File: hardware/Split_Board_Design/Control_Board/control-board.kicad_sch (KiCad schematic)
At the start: 12 parts, among them J10 Conn_01x03, J2 UART_CONN, J3 XT30PW-M, J5 Conn_01x06, J7 Conn_01x03, J8 Conn_01x03, J9 Conn_01x02

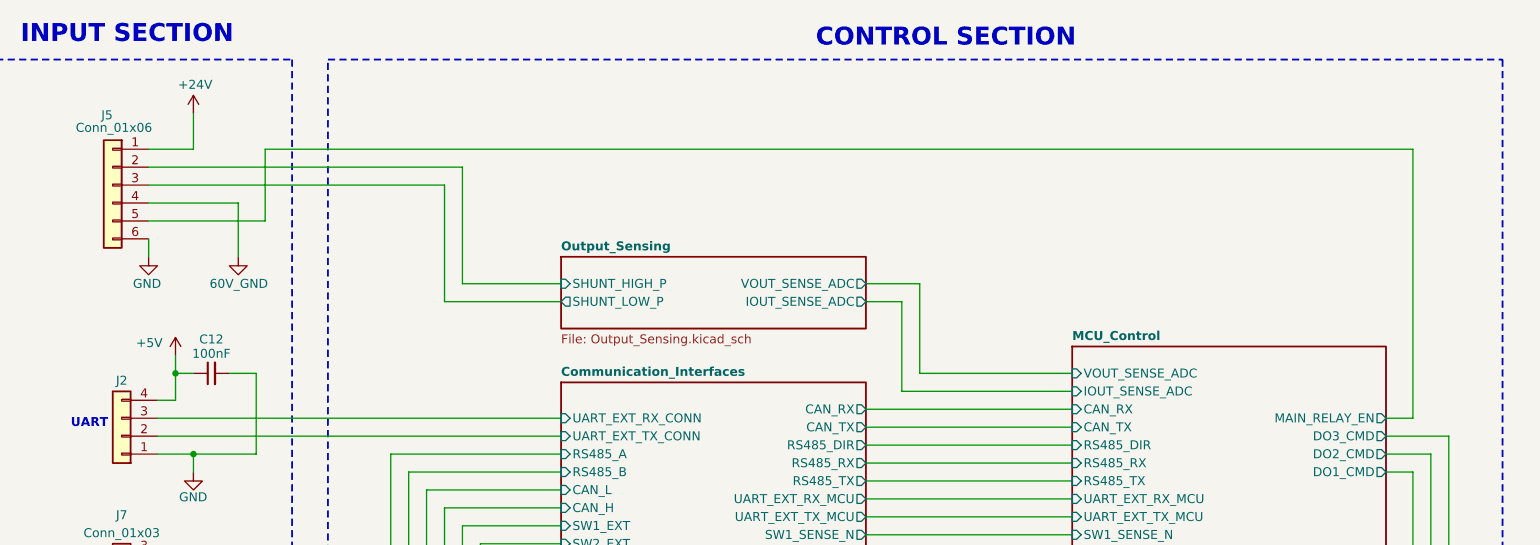
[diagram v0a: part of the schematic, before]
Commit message: feat(layout): Finished demo schematic for control board
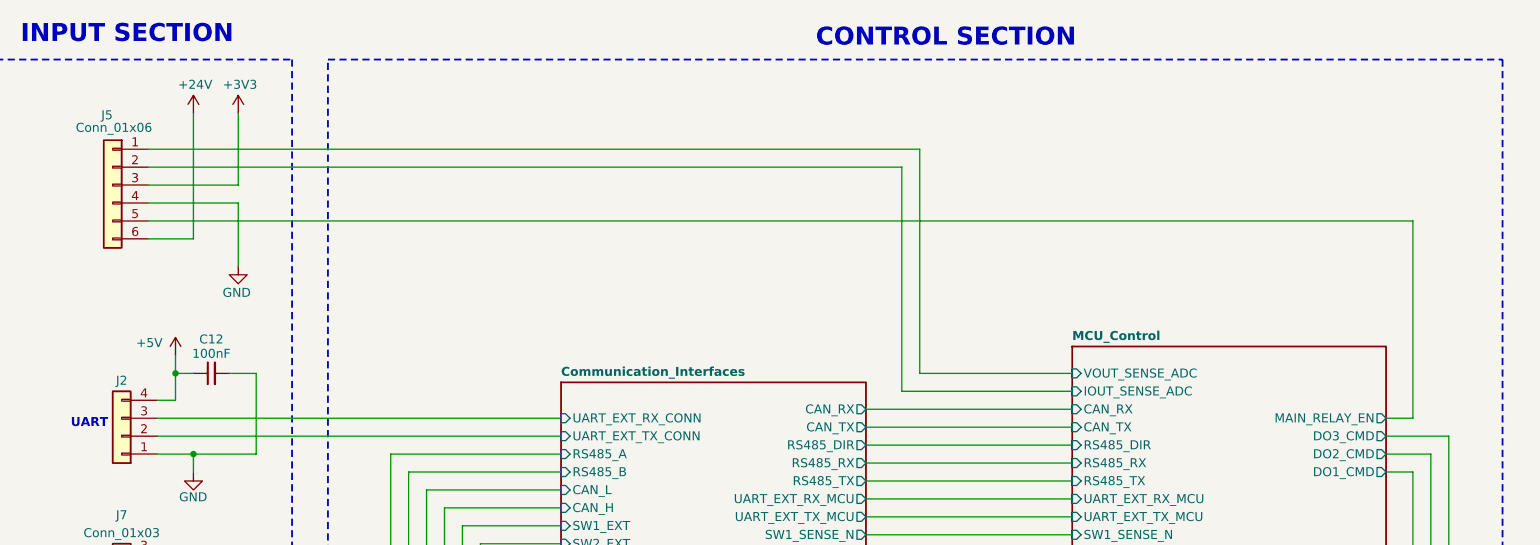
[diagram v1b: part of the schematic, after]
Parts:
- J10, J7: footprint Connector_Phoenix_MC:PhoenixContact_MC_1,5_3-G-3.5_1x03_P3.50mm_Horizontal -> Connector_Phoenix_MC:PhoenixContact_MC_1,5_3-G-3.81_1x03_P3.81mm_Horizontal; Link to Buy (none) -> https://linhkien.cxtvn.com/3486-cau-dau-15edg381-381mm-xanh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
- J5: Link to Buy (none) -> https://linhkien.cxtvn.com/3878-header-duc-xh254-6p-chan-co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
- J8, J9: Link to Buy (none) -> https://linhkien.cxtvn.com/3486-cau-dau-15edg381-381mm-xanh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
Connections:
- net 60V_GND is gone; now on net GND: J5.4 (Pin_4)
- net Output_Sensing/SHUNT_HIGH_P is gone; now on net MCU_Control/IOUT_SENSE_ADC: J5.2 (Pin_2)
- net Output_Sensing/SHUNT_LOW_P is gone; now on net +3V3: J5.3 (Pin_3)
- net +24V: now also J5.6 (Pin_6); no longer J5.1 (Pin_1)
- net GND: no longer J5.6 (Pin_6)
- net MCU_Control/VOUT_SENSE_ADC: now also J5.1 (Pin_1)
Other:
- removed sheet Output_Sensing

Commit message: feat(layout): Update layout
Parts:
- C12: value 100nF -> 100nF-50V; footprint Capacitor_SMD:C_0805_2012Metric -> Capacitor_SMD:C_0603_1608Metric; Link to Buy https://linhkien.cxtvn.com/1976-tu-khong-phan-cuc-0805.html -> https://linhkien.cxtvn.com/1981-tu-0603-khong-phan-cuc.html
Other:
- moved on the sheet: H4, H5, H6, H7
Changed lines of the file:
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@@
 	(wire
 		(pts
-			(xy 146.05 38.1) (xy 36.83 38.1)
+			(xy 153.67 38.1) (xy 36.83 38.1)
 		)
 		(stroke
@@
 	(wire
 		(pts
-			(xy 143.51 72.39) (xy 167.64 72.39)
+			(xy 151.13 72.39) (xy 167.64 72.39)
 		)
 		(stroke
@@
 	(wire
 		(pts
-			(xy 146.05 69.85) (xy 167.64 69.85)
+			(xy 153.67 69.85) (xy 167.64 69.85)
 		)
 		(stroke
@@
 	(wire
 		(pts
-			(xy 143.51 40.64) (xy 143.51 72.39)
+			(xy 151.13 40.64) (xy 151.13 72.39)
 		)
 		(stroke
@@
 	(wire
 		(pts
-			(xy 143.51 40.64) (xy 36.83 40.64)
+			(xy 151.13 40.64) (xy 36.83 40.64)
 		)
 		(stroke
@@
 	(wire
 		(pts
-			(xy 146.05 38.1) (xy 146.05 69.85)
+			(xy 153.67 38.1) (xy 153.67 69.85)
 		)
 		(stroke
@@
 	(symbol
 		(lib_id "Mechanical:MountingHole")
-		(at 99.06 173.99 0)
+		(at 99.06 182.88 0)
 		(unit 1)
 		(body_style 1)
@@
 		(fields_autoplaced yes)
 		(property "Reference" "H7"
-			(at 101.6 172.7199 0)
+			(at 101.6 181.6099 0)
 			(show_name no)
 			(do_not_autoplace no)
@@
 		)
 		(property "Value" "MountingHole"
-			(at 101.6 175.2599 0)
+			(at 101.6 184.1499 0)
 			(show_name no)
 			(do_not_autoplace no)
@@
 		)
 		(property "Footprint" "MountingHole:MountingHole_3.2mm_M3"
-			(at 99.06 173.99 0)
+			(at 99.06 182.88 0)
 			(hide yes)
 			(show_name no)
@@
 		)
 		(property "Datasheet" ""
-			(at 99.06 173.99 0)
+			(at 99.06 182.88 0)
 			(hide yes)
 			(show_name no)
@@
 		)
 		(property "Description" "Mounting Hole without connection"
-			(at 99.06 173.99 0)
+			(at 99.06 182.88 0)
 			(hide yes)
 			(show_name no)
@@
 		)
 		(property "CREATOR" ""
-			(at 99.06 173.99 0)
+			(at 99.06 182.88 0)
 			(hide yes)
 			(show_name no)
@@
 	(symbol
 		(lib_id "Mechanical:MountingHole")
-		(at 157.48 173.99 0)
+		(at 157.48 182.88 0)
 		(unit 1)
 		(body_style 1)
@@
 		(fields_autoplaced yes)
 		(property "Reference" "H4"
-			(at 160.02 172.7199 0)
+			(at 160.02 181.6099 0)
 			(show_name no)
 			(do_not_autoplace no)
@@
 		)
 		(property "Value" "MountingHole"
-			(at 160.02 175.2599 0)
+			(at 160.02 184.1499 0)
 			(show_name no)
 			(do_not_autoplace no)
@@
 		)
 		(property "Footprint" "MountingHole:MountingHole_3.2mm_M3"
-			(at 157.48 173.99 0)
+			(at 157.48 182.88 0)
 			(hide yes)
 			(show_name no)
@@
 		)
 		(property "Datasheet" ""
-			(at 157.48 173.99 0)
+			(at 157.48 182.88 0)
 			(hide yes)
 			(show_name no)
@@
 		)
 		(property "Description" "Mounting Hole without connection"
-			(at 157.48 173.99 0)
+			(at 157.48 182.88 0)
 			(hide yes)
 			(show_name no)
@@
 		)
 		(property "CREATOR" ""
-			(at 157.48 173.99 0)
+			(at 157.48 182.88 0)
 			(hide yes)
 			(show_name no)
@@
 	(symbol
 		(lib_id "Mechanical:MountingHole")
-		(at 118.11 173.99 0)
+		(at 118.11 182.88 0)
 		(unit 1)
 		(body_style 1)
@@
 		(fields_autoplaced yes)
 		(property "Reference" "H6"
-			(at 120.65 172.7199 0)
+			(at 120.65 181.6099 0)
 			(show_name no)
 			(do_not_autoplace no)
@@
 		)
 		(property "Value" "MountingHole"
-			(at 120.65 175.2599 0)
+			(at 120.65 184.1499 0)
 			(show_name no)
 			(do_not_autoplace no)
@@
 		)
 		(property "Footprint" "MountingHole:MountingHole_3.2mm_M3"
-			(at 118.11 173.99 0)
+			(at 118.11 182.88 0)
 			(hide yes)
 			(show_name no)
@@
 		)
 		(property "Datasheet" ""
-			(at 118.11 173.99 0)
+			(at 118.11 182.88 0)
 			(hide yes)
 			(show_name no)
@@
 		)
 		(property "Description" "Mounting Hole without connection"
-			(at 118.11 173.99 0)
+			(at 118.11 182.88 0)
 			(hide yes)
 			(show_name no)
@@
 		)
 		(property "CREATOR" ""
-			(at 118.11 173.99 0)
+			(at 118.11 182.88 0)
 			(hide yes)
 			(show_name no)
@@
 			)
 		)
-		(property "Value" "100nF"
+		(property "Value" "100nF-50V"
 			(at 45.72 67.056 90)
 			(show_name no)
@@
 			)
 		)
-		(property "Footprint" "Capacitor_SMD:C_0805_2012Metric"
+		(property "Footprint" "Capacitor_SMD:C_0603_1608Metric"
 			(at 45.72 69.85 0)
 			(hide yes)
@@
 			)
 		)
-		(property "Link to Buy" "https://linhkien.cxtvn.com/1976-tu-khong-phan-cuc-0805.html"
+		(property "Link to Buy" "https://linhkien.cxtvn.com/1981-tu-0603-khong-phan-cuc.html"
 			(at -80.01 179.07 0)
 			(hide yes)
@@
 	(symbol
 		(lib_id "Mechanical:MountingHole")
-		(at 137.16 173.99 0)
+		(at 137.16 182.88 0)
 		(unit 1)
 		(body_style 1)
@@
 		(fields_autoplaced yes)
 		(property "Reference" "H5"
-			(at 139.7 172.7199 0)
+			(at 139.7 181.6099 0)
 			(show_name no)
 			(do_not_autoplace no)
@@
 		)
 		(property "Value" "MountingHole"
-			(at 139.7 175.2599 0)
+			(at 139.7 184.1499 0)
 			(show_name no)
 			(do_not_autoplace no)
@@
 		)
 		(property "Footprint" "MountingHole:MountingHole_3.2mm_M3"
-			(at 137.16 173.99 0)
+			(at 137.16 182.88 0)
 			(hide yes)
 			(show_name no)
@@
 		)
 		(property "Datasheet" ""
-			(at 137.16 173.99 0)
+			(at 137.16 182.88 0)
 			(hide yes)
 			(show_name no)
@@
 		)
 		(property "Description" "Mounting Hole without connection"
-			(at 137.16 173.99 0)
+			(at 137.16 182.88 0)
 			(hide yes)
 			(show_name no)
@@
 		)
 		(property "CREATOR" ""
-			(at 137.16 173.99 0)
+			(at 137.16 182.88 0)
 			(hide yes)
 			(show_name no)

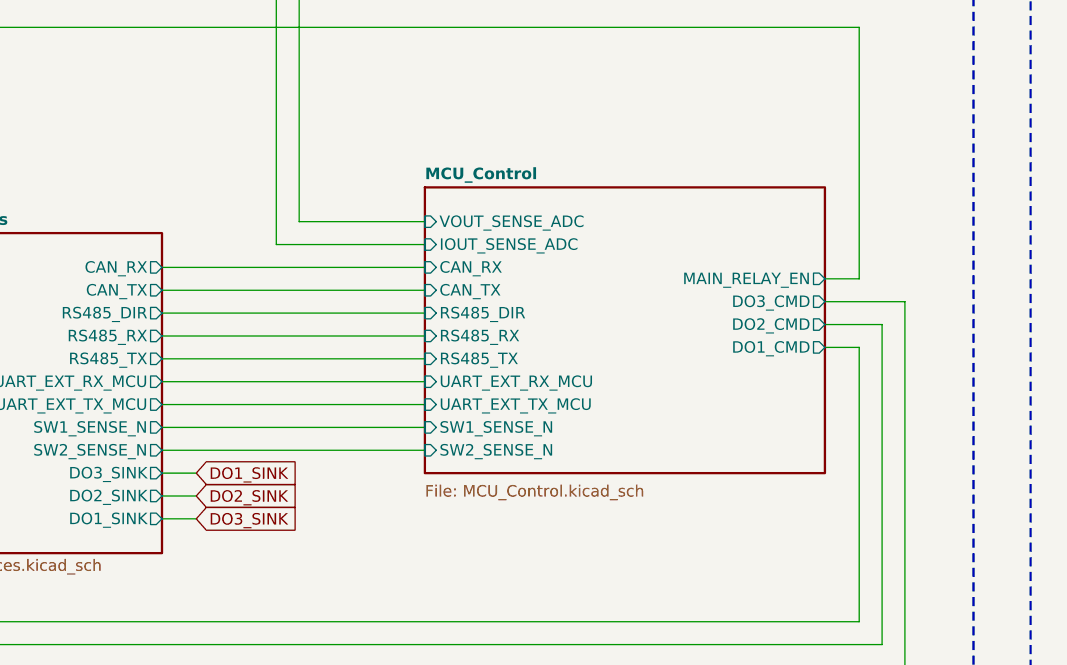
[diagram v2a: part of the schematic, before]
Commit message: feat(layout): update control board layout
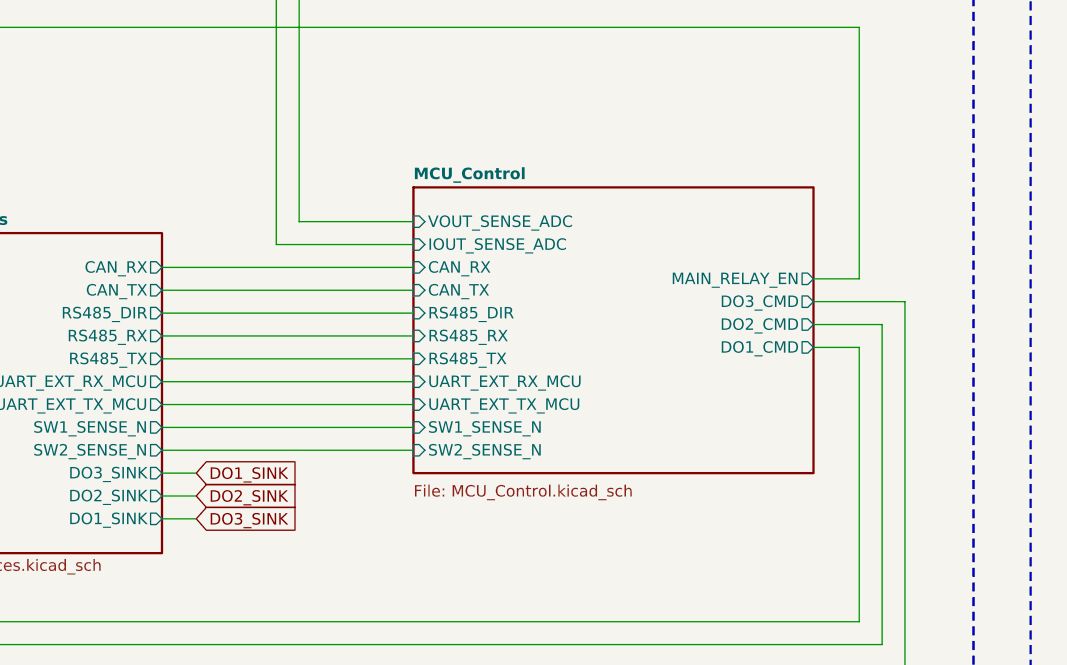
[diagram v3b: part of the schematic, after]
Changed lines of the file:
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@@
 	(wire
 		(pts
-			(xy 212.09 78.74) (xy 220.98 78.74)
+			(xy 210.82 78.74) (xy 220.98 78.74)
 		)
 		(stroke
@@
 	(wire
 		(pts
-			(xy 151.13 72.39) (xy 167.64 72.39)
+			(xy 151.13 72.39) (xy 166.37 72.39)
 		)
 		(stroke
@@
 	(wire
 		(pts
-			(xy 167.64 80.01) (xy 138.43 80.01)
+			(xy 166.37 80.01) (xy 138.43 80.01)
 		)
 		(stroke
@@
 	(wire
 		(pts
-			(xy 153.67 69.85) (xy 167.64 69.85)
+			(xy 153.67 69.85) (xy 166.37 69.85)
 		)
 		(stroke
@@
 	(wire
 		(pts
-			(xy 167.64 85.09) (xy 138.43 85.09)
+			(xy 166.37 85.09) (xy 138.43 85.09)
 		)
 		(stroke
@@
 	(wire
 		(pts
-			(xy 167.64 82.55) (xy 138.43 82.55)
+			(xy 166.37 82.55) (xy 138.43 82.55)
 		)
 		(stroke
@@
 	(wire
 		(pts
-			(xy 215.9 76.2) (xy 212.09 76.2)
+			(xy 215.9 76.2) (xy 210.82 76.2)
 		)
 		(stroke
@@
 	(wire
 		(pts
-			(xy 167.64 92.71) (xy 138.43 92.71)
+			(xy 166.37 92.71) (xy 138.43 92.71)
 		)
 		(stroke
@@
 	(wire
 		(pts
-			(xy 167.64 95.25) (xy 138.43 95.25)
+			(xy 166.37 95.25) (xy 138.43 95.25)
 		)
 		(stroke
@@
 	(wire
 		(pts
-			(xy 167.64 74.93) (xy 138.43 74.93)
+			(xy 166.37 74.93) (xy 138.43 74.93)
 		)
 		(stroke
@@
 	(wire
 		(pts
-			(xy 167.64 87.63) (xy 138.43 87.63)
+			(xy 166.37 87.63) (xy 138.43 87.63)
 		)
 		(stroke
@@
 	(wire
 		(pts
-			(xy 212.09 81.28) (xy 218.44 81.28)
+			(xy 210.82 81.28) (xy 218.44 81.28)
 		)
 		(stroke
@@
 	(wire
 		(pts
-			(xy 212.09 83.82) (xy 215.9 83.82)
+			(xy 210.82 83.82) (xy 215.9 83.82)
 		)
 		(stroke
@@
 	(wire
 		(pts
-			(xy 167.64 77.47) (xy 138.43 77.47)
+			(xy 166.37 77.47) (xy 138.43 77.47)
 		)
 		(stroke
@@
 	(wire
 		(pts
-			(xy 167.64 90.17) (xy 138.43 90.17)
+			(xy 166.37 90.17) (xy 138.43 90.17)
 		)
 		(stroke
@@
 	)
 	(sheet
-		(at 167.64 66.04)
+		(at 166.37 66.04)
 		(size 44.45 31.75)
 		(exclude_from_sim no)
@@
 		)
 		(property "Sheetname" "MCU_Control"
-			(at 167.64 65.2776 0)
+			(at 166.37 65.2776 0)
 			(show_name no)
 			(do_not_autoplace no)
@@
 		)
 		(property "Sheetfile" "MCU_Control.kicad_sch"
-			(at 167.64 99.06 0)
+			(at 166.37 99.06 0)
 			(show_name no)
 			(do_not_autoplace no)
@@
 		)
 		(pin "IOUT_SENSE_ADC" input
-			(at 167.64 72.39 180)
+			(at 166.37 72.39 180)
 			(effects
 				(font
@@
 		)
 		(pin "MAIN_RELAY_EN" output
-			(at 212.09 76.2 0)
+			(at 210.82 76.2 0)
 			(effects
 				(font
@@
 		)
 		(pin "VOUT_SENSE_ADC" input
-			(at 167.64 69.85 180)
+			(at 166.37 69.85 180)
 			(effects
 				(font
@@
 		)
 		(pin "CAN_RX" input
-			(at 167.64 74.93 180)
+			(at 166.37 74.93 180)
 			(effects
 				(font
@@
 		)
 		(pin "RS485_DIR" input
-			(at 167.64 80.01 180)
+			(at 166.37 80.01 180)
 			(effects
 				(font
@@
 		)
 		(pin "CAN_TX" input
-			(at 167.64 77.47 180)
+			(at 166.37 77.47 180)
 			(effects
 				(font
@@
 		)
 		(pin "RS485_RX" input
-			(at 167.64 82.55 180)
+			(at 166.37 82.55 180)
 			(effects
 				(font
@@
 		)
 		(pin "RS485_TX" input
-			(at 167.64 85.09 180)
+			(at 166.37 85.09 180)
 			(effects
 				(font
@@
 		)
 		(pin "UART_EXT_RX_MCU" input
-			(at 167.64 87.63 180)
+			(at 166.37 87.63 180)
 			(effects
 				(font
@@
 		)
 		(pin "UART_EXT_TX_MCU" input
-			(at 167.64 90.17 180)
+			(at 166.37 90.17 180)
 			(effects
 				(font
@@
 		)
 		(pin "DO1_CMD" output
-			(at 212.09 83.82 0)
+			(at 210.82 83.82 0)
 			(effects
 				(font
@@
 		)
 		(pin "DO2_CMD" output
-			(at 212.09 81.28 0)
+			(at 210.82 81.28 0)
 			(effects
 				(font
@@
 		)
 		(pin "DO3_CMD" output
-			(at 212.09 78.74 0)
+			(at 210.82 78.74 0)
 			(effects
 				(font
@@
 		)
 		(pin "SW1_SENSE_N" input
-			(at 167.64 92.71 180)
+			(at 166.37 92.71 180)
 			(effects
 				(font
@@
 		)
 		(pin "SW2_SENSE_N" input
-			(at 167.64 95.25 180)
+			(at 166.37 95.25 180)
 			(effects
 				(font

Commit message: layout: update layout
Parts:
- removed J3: XT30PW-M, RobotChargeController:AMASS_XT30PW-M, symbol RobotChargeController:XT30PW-M
- added J11: Conn_01x02, Connector_Phoenix_MC:PhoenixContact_MC_1,5_2-G-3.81_1x02_P3.81mm_Horizontal, symbol Connector_Generic:Conn_01x02
- J2: footprint Connector_JST:JST_XH_S4B-XH-A-1_1x04_P2.50mm_Horizontal -> RobotChargeController:JST_XH_S4B-XH-A-1_1x04_P2.50mm_Horizontal
- J5: footprint Connector_JST:JST_XH_S6B-XH-A_1x06_P2.50mm_Horizontal -> RobotChargeController:JST_XH_S6B-XH-A_1x06_P2.50mm_Horizontal
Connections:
- net +24V is gone; now on net GND: J5.6 (Pin_6)
- net Auxiliary_Power_Supply/VAUX_IN_P: now also J11.2 (Pin_2)
- net GND: now also J11.1 (Pin_1)
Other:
- moved on the sheet: C12
